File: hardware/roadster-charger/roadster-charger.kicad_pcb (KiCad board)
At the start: 4 copper layers, 74.7 x 50.2 mm, 93 parts, among them J1 USB4505-03-0-A, J2 USB4505-03-0-A, J3 54-00166, Q1 CSD19532Q5B, Q2 CSD19532Q5B, Q3 CSD19532Q5B, U1 FUSB307BMPX, U10 OPA340NA, U11 LM75B, U2 ESP32-C3-MINI-1, U3 INA168, U4 LM5050-1, U5 INA168, U6 OPA340NA, U7 DAC70501MDQFR, U8 LTC3786EUD#TRPBF, U9 MPM3606AGQV-P

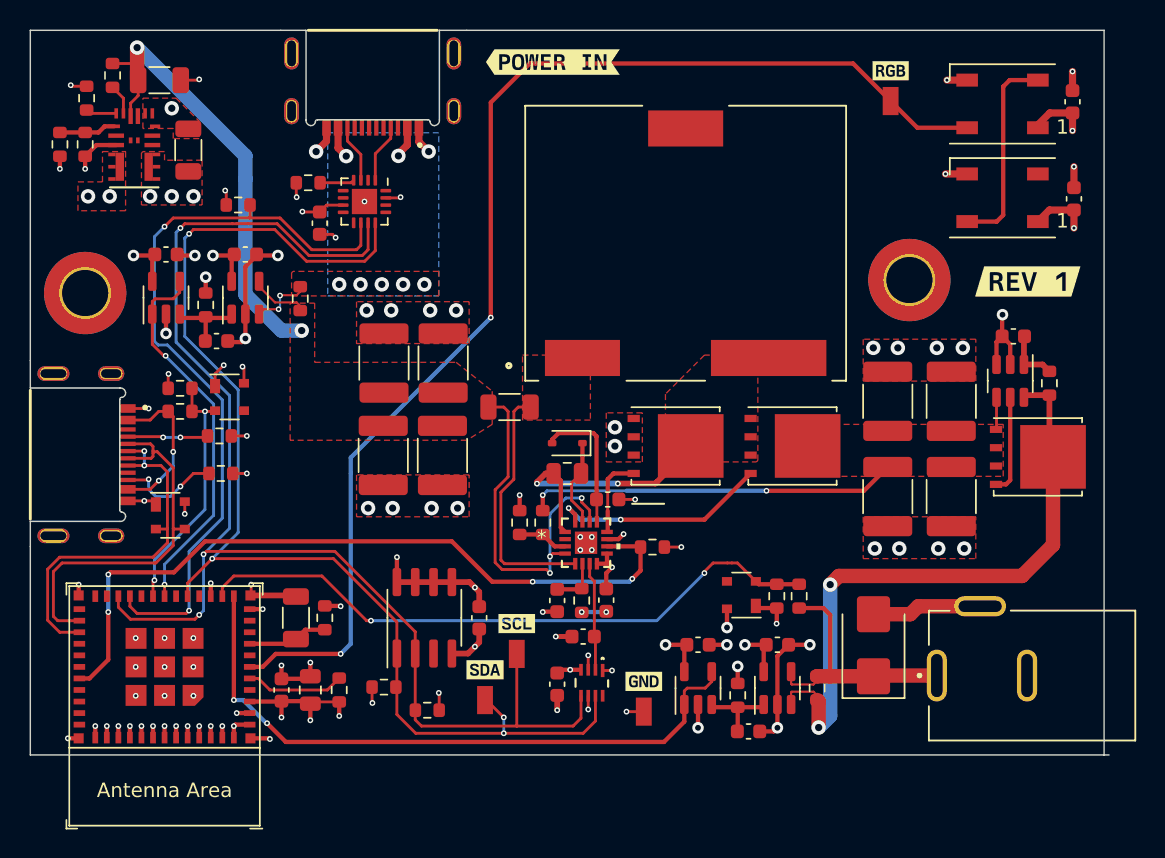
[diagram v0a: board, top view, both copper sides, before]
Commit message: clean up debug USB-C port components
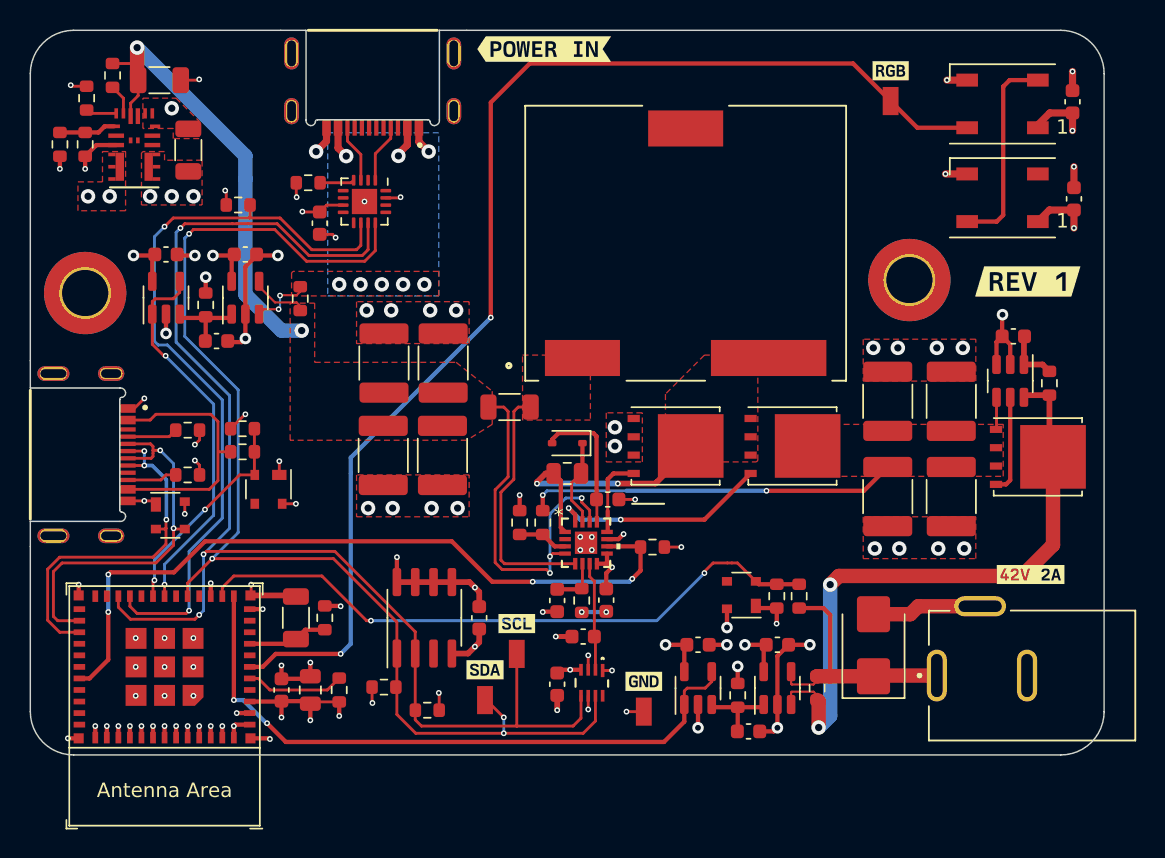
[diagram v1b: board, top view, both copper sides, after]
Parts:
- added kibuzzard-657BC539: G***, kibuzzard-657BC539, F.Cu at (251.6, 147.0)
- moved D4 6.95 mm to (198.8, 141.1), turned to -90 degrees
- moved R23 5.15 mm to (197.0, 138.5)
- moved R24 5.15 mm to (197.0, 136.9)
- moved R8 2.30 mm to (193.2, 140.1)
- moved R6 2.24 mm to (193.2, 137.0)
- moved kibuzzard-657BB0E9 1.08 mm to (217.9, 110.6)
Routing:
- net /DBG_VBUS: track 10.8 -> 18.0 mm, vias 2 -> 0
- net Net-(J2-CC2): track 7.22 -> 3.47 mm, vias 2 -> 0
- net /DBG_DETECT: track 17.5 -> 15.1 mm
- net Net-(J2-CC1): track 5.59 -> 3.51 mm, vias 2 -> 0
- net /USB_DP: track 25.9 -> 25.4 mm, vias 2 -> 3
- net /USB_DM: track 26.5 -> 26.7 mm, vias 0 -> 2
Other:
- board size 74.7 x 50.2 mm -> 74.4 x 50.2 mm

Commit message: add charger image to back
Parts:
- added G***: LOGO, LOGO, B.Cu at (227.0, 123.6)

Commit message: run schematic annotation to clean up error
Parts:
- H1, H2: value MountingHole -> MountingHole_Pad
- moved H1 57.1 mm to (186.1, 127.5)
- moved H2 57.1 mm to (243.2, 126.6)
- renumbered C4 to C10, C5 to C11, C22 to C12, C8 to C13, C9 to C14, C21 to C15, C6 to C16, C23 to C17, C24 to C18, C25 to C19, C26 to C20, C31 to C21, C32 to C22, C14 to C23, C33 to C24, C15 to C25, C7 to C26, C12 to C27, C16 to C28, C13 to C29, C10 to C3, C17 to C30, C3 to C4, C18 to C5, C11 to C6, C20 to C7, C27 to C8, C19 to C9, D5 to D4, D4 to D5, D7 to D6, D6 to D7, L2 to L1, Q3 to Q2, Q2 to Q3, R5 to R1, R2 to R10, R3 to R11, R4 to R12, R9 to R13, R12 to R14, R13 to R15, R8 to R16, R6 to R17, R10 to R18, R11 to R19, R19 to R2, R23 to R20, R24 to R21, R14 to R22, R15 to R23, R16 to R24, R17 to R25, R18 to R26, R21 to R3, R26 to R4, R20 to R5, R25 to R6, R22 to R7, R7 to R8, R1 to R9, TP4 to TP1, TP1 to TP2, TP2 to TP3, TP3 to TP4, U9 to U1, U7 to U10, U8 to U11, U10 to U4, U1 to U5, U11 to U6, U4 to U7, U5 to U8, U6 to U9
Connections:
- H1 pad 1: (no net) -> GND
- H2 pad 1: (no net) -> GND

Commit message: clean up fab layer, add value to test points
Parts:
- TP1, TP2, TP3, TP4: value TestPoint -> RCU-0C

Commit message: add note to DAC circuit, swap DAC to model with 0V output at boot
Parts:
- U10: value DAC70501MDQFR -> DAC70501ZDQFT
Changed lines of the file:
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@@
     (at 221.2 154.5 -90)
     (tags "DAC70501MDQFR ")
-    (property "MPN" "DAC70501MDQFR")
+    (property "MPN" "DAC70501ZDQFT")
     (property "Sheetfile" "boost.kicad_sch")
     (property "Sheetname" "boost")
@@
         (effects (font (size 1 1) (thickness 0.15)))
     )
-    (fp_text value "DAC70501MDQFR" (at 0 0 -90 unlocked) (layer "F.Fab") hide
+    (fp_text value "DAC70501ZDQFT" (at 0 0 -90 unlocked) (layer "F.Fab") hide
         (effects (font (size 1 1) (thickness 0.15)))
     )

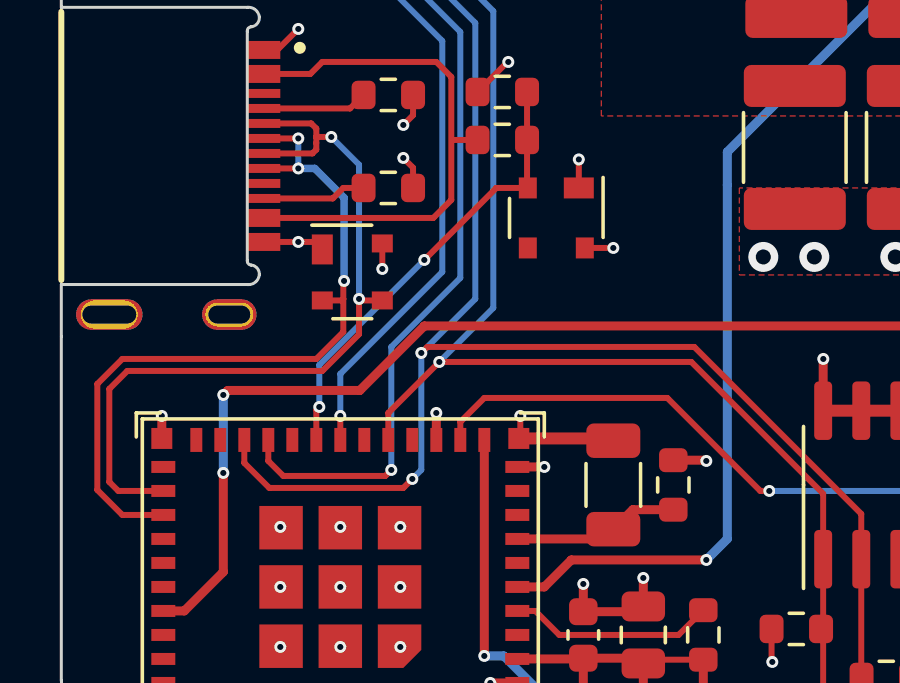
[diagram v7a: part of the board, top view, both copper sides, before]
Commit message: add IO9 test point for when I accidentally reassign usb pins during fw dev
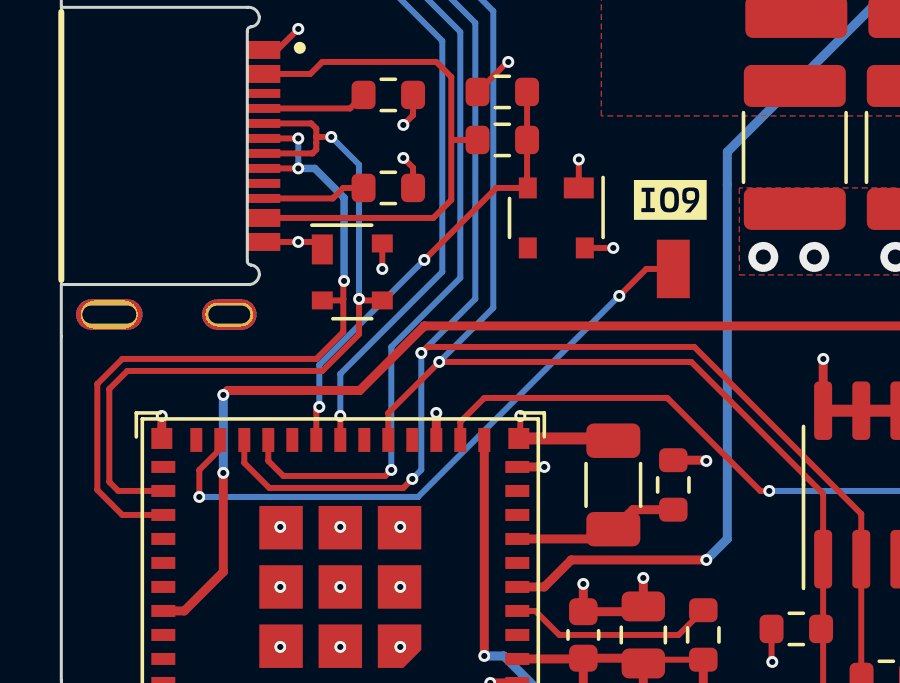
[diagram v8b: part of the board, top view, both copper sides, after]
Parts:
- added TP1: RCU-0C, RCU-0C:TP+195X110, F.Cu at (202.7, 142.8)
- added kibuzzard-657FB5DD: G***, kibuzzard-657FB5DD, F.Cu at (202.6, 140.5)
- renumbered TP1 to TP2, TP2 to TP3, TP3 to TP4, TP4 to TP5
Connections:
- U2 pad 23: unconnected-(U2-GPIO9-Pad23) -> /IO9_BOOT
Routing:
- net /IO9_BOOT: track 0.00 -> 21.1 mm, vias 0 -> 2
